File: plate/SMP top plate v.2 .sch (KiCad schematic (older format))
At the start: 4 parts

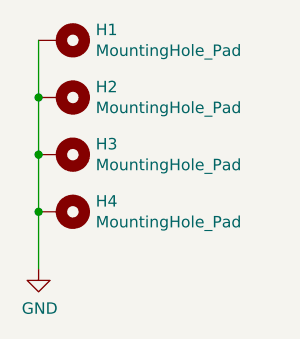
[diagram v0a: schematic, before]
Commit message: update top plate
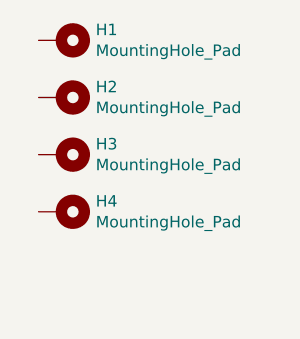
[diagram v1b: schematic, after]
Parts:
- H1, H2, H3, H4: footprint MountingHole:MountingHole_2.2mm_M2_Pad_TopBottom -> MountingHole:MountingHole_3.2mm_M3_Pad_TopBottom
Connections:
- removed net GND: H1.1, H2.1, H3.1, H4.1
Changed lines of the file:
@@
 F 0 "H2" V 3654 3450 50  0000 L CNN
 F 1 "MountingHole_Pad" V 3745 3450 50  0000 L CNN
-F 2 "MountingHole:MountingHole_2.2mm_M2_Pad_TopBottom" H 3700 3300 50  0001 C CNN
+F 2 "MountingHole:MountingHole_3.2mm_M3_Pad_TopBottom" H 3700 3300 50  0001 C CNN
 F 3 "~" H 3700 3300 50  0001 C CNN
 	1    3700 3300
@@
 F 0 "H3" V 3654 3700 50  0000 L CNN
 F 1 "MountingHole_Pad" V 3745 3700 50  0000 L CNN
-F 2 "MountingHole:MountingHole_2.2mm_M2_Pad_TopBottom" H 3700 3550 50  0001 C CNN
+F 2 "MountingHole:MountingHole_3.2mm_M3_Pad_TopBottom" H 3700 3550 50  0001 C CNN
 F 3 "~" H 3700 3550 50  0001 C CNN
 	1    3700 3550
@@
 F 0 "H1" V 3654 3200 50  0000 L CNN
 F 1 "MountingHole_Pad" V 3745 3200 50  0000 L CNN
-F 2 "MountingHole:MountingHole_2.2mm_M2_Pad_TopBottom" H 3700 3050 50  0001 C CNN
+F 2 "MountingHole:MountingHole_3.2mm_M3_Pad_TopBottom" H 3700 3050 50  0001 C CNN
 F 3 "~" H 3700 3050 50  0001 C CNN
 	1    3700 3050
@@
 F 0 "H4" V 3654 3950 50  0000 L CNN
 F 1 "MountingHole_Pad" V 3745 3950 50  0000 L CNN
-F 2 "MountingHole:MountingHole_2.2mm_M2_Pad_TopBottom" H 3700 3800 50  0001 C CNN
+F 2 "MountingHole:MountingHole_3.2mm_M3_Pad_TopBottom" H 3700 3800 50  0001 C CNN
 F 3 "~" H 3700 3800 50  0001 C CNN
 	1    3700 3800
 	0    1    1    0
 $EndComp
-$Comp
-L power:GND #PWR0101
-U 1 1 611D224B
-P 3600 4050
-F 0 "#PWR0101" H 3600 3800 50  0001 C CNN
-F 1 "GND" H 3605 3877 50  0000 C CNN
-F 2 "" H 3600 4050 50  0001 C CNN
-F 3 "" H 3600 4050 50  0001 C CNN
-	1    3600 4050
-	1    0    0    -1
-$EndComp
-Wire Wire Line
-	3600 3050 3600 3300
-Connection ~ 3600 3300
-Wire Wire Line
-	3600 3300 3600 3550
-Connection ~ 3600 3550
-Wire Wire Line
-	3600 3550 3600 3800
-Connection ~ 3600 3800
-Wire Wire Line
-	3600 3800 3600 4050
 $EndSCHEMATC
